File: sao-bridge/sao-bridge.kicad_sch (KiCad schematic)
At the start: 6 parts, among them J1 SAO_LEFT, J2 BADGE_LEFT, J3 SAO_MID, J4 BADGE_RIGHT, J5 SAO_RIGHT, J6 GPIO_MID

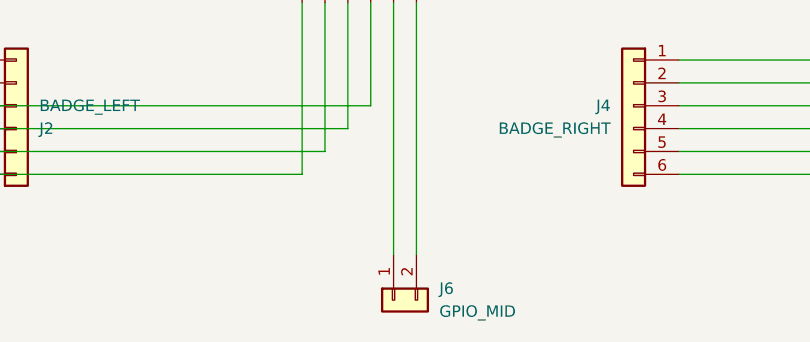
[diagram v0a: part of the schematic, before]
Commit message: add some info to bottom siklscreen
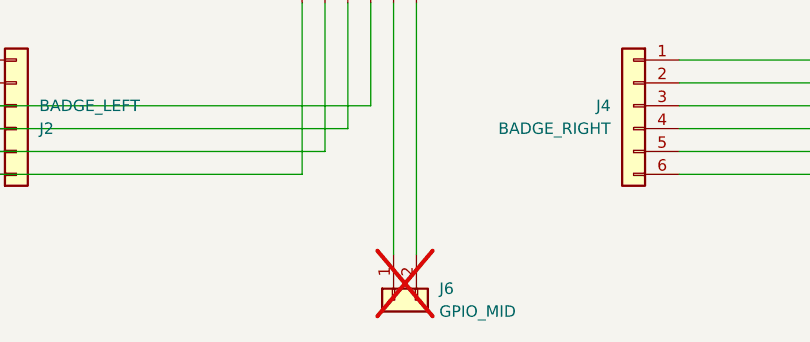
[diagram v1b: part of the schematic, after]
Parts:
- J6: now not fitted
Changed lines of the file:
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@@
 		(in_bom yes)
 		(on_board yes)
-		(dnp no)
+		(dnp yes)
 		(fields_autoplaced yes)
 		(property "Reference" "J6"
